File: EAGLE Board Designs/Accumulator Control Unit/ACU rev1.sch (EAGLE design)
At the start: 187 parts, among them J1 CONNECTOR-CAN_MF_T_V_, J2 CONNECTOR-8_MF_T_V_, J3 CONNECTOR-8_MF_T_V_, J4 CONNECTOR-2_MF_T_V_, J5 CONNECTOR-12_MF_T_V_, Q1 TRANSISTOR_N_MOS__PMV15ENEA, Q2 TRANSISTOR_N_MOS__PMV15ENEA, T1 TRANSFORMER_HM2112ZNLT_AIRGAP, U10 OPAMP_1_CHANNEL_OPA991, U11 LOGICGATE_AND_DCK3, U12 OPAMP_1_CHANNEL_OPA991, U13 OPAMP_1_CHANNEL_OPA991, U14 OPAMP_1_CHANNEL_OPA991, U15 LOGICGATE_AND_DCK3, U18 OPAMP_1_CHANNEL_OPA991, U19 MAX7404, U2 ADG1423, U20 OPAMP_1_CHANNEL_OPA991, U22 OPAMP_1_CHANNEL_OPA991, U25 TCAN1051HQV-Q1, U26 MAX7404, U27 OPAMP_1_CHANNEL_OPA991, U28 MAX7404, U29 OPAMP_1_CHANNEL_OPA991, U3 LM555, U30 MAX7404, U4 OPAMP_1_CHANNEL_OPA991, U5 LTC6820, U6 ADM823, U7 OPAMP_1_CHANNEL_OPA991, U8 LOGICGATE_AND_DCK3, U9 OPAMP_1_CHANNEL_OPA991

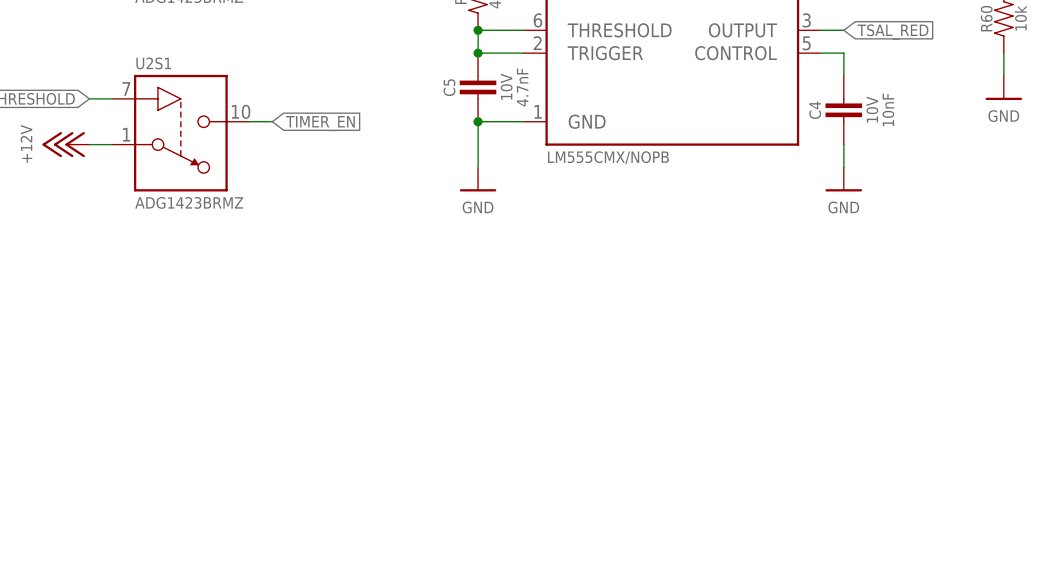
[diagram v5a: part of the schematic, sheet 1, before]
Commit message: Corrections
Added isolation barrier line
moved LTC6820 near teensy
moved precharger near connector
shdn traces now 20 mil
removed unneeded vias near 3.3V reg
mvoed caps of vregs inside keepouts
added 0603 LEDs for TSAL
mapped can tx and rx to D3 and D4 for compatibility with Teensy 3.2
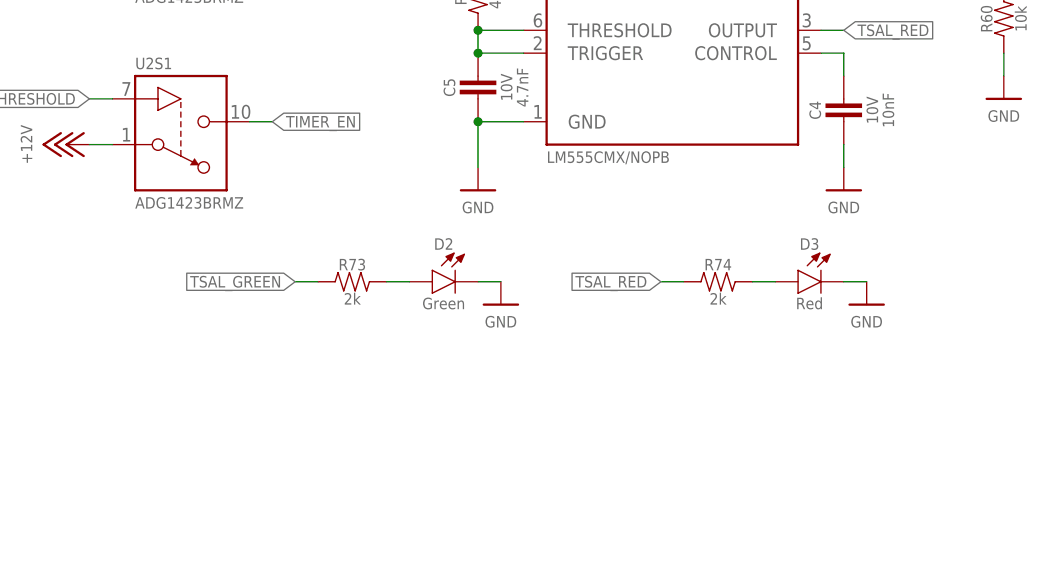
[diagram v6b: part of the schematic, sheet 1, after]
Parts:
- added D2: LED_0603_GREEN, HyTechDevices:LED_0603_GREEN
- added D3: LED_0603_RED, HyTechDevices:LED_0603_RED
- added R73, R74: RESISTOR_0603_2K, HyTechDevices:RESISTOR_0603_2K
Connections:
- new net N$29: A1.(CTX1)D1, A1.D3, U25.TXD
- new net N$46: D3.A, R74.2
- net GND: now also D2.C, D3.C
- net N$24: now also D2.A, R73.2; no longer A1.(CTX1)D1, U25.TXD
- net N$25: now also A1.D4
- net TEENSY_OK: now also A1.D6; no longer A1.D5
- net TSAL_GREEN: now also R73.1
- net TSAL_RED: now also R74.1
- net WATCHDOG_INPUT: now also A1.D5; no longer A1.D4
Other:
- moved on the sheet: WATCHDOG_OK
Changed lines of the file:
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@@
 <drawing>
 <settings>
-<setting alwaysvectorfont="yes"/>
+<setting alwaysvectorfont="no"/>
 <setting verticaltext="up"/>
 </settings>
@@
 <part name="IMD_OK" library="HyTechDevices - Copy" deviceset="LED_?_*" device="0603" technology="ORANGE"/>
 <part name="R72" library="HyTechDevices" deviceset="RESISTOR_?_*" device="0603" technology="2K"/>
+<part name="D2" library="HyTechDevices" deviceset="LED_?_*" device="0603" technology="GREEN"/>
+<part name="D3" library="HyTechDevices" deviceset="LED_?_*" device="0603" technology="RED"/>
+<part name="R73" library="HyTechDevices" deviceset="RESISTOR_?_*" device="0603" technology="2K"/>
+<part name="R74" library="HyTechDevices" deviceset="RESISTOR_?_*" device="0603" technology="2K"/>
+<part name="P48" library="HyTechSupplies" deviceset="GND" device=""/>
+<part name="P49" library="HyTechSupplies" deviceset="GND" device=""/>
 </parts>
 <sheets>
@@
 <attribute name="MPN" x="17.78" y="79.502" size="1.27" layer="95" align="top-left"/>
 </instance>
+<instance part="D2" gate="LED" x="190.5" y="66.04" smashed="yes">
+<attribute name="COLOR" x="189.23" y="64.262" size="1.27" layer="95" align="top-center"/>
+<attribute name="NAME" x="189.23" y="69.596" size="1.27" layer="96" align="bottom-center"/>
+</instance>
+<instance part="D3" gate="LED" x="231.14" y="66.04" smashed="yes">
+<attribute name="COLOR" x="229.87" y="64.262" size="1.27" layer="95" align="top-center"/>
+<attribute name="NAME" x="229.87" y="69.596" size="1.27" layer="96" align="bottom-center"/>
+</instance>
+<instance part="R73" gate="G$1" x="180.34" y="66.04" smashed="yes">
+<attribute name="NAME" x="179.07" y="67.31" size="1.27" layer="95" align="bottom-center"/>
+<attribute name="RESISTANCE" x="179.07" y="64.77" size="1.27" layer="96" align="top-center"/>
+</instance>
+<instance part="R74" gate="G$1" x="220.98" y="66.04" smashed="yes">
+<attribute name="NAME" x="219.71" y="67.31" size="1.27" layer="95" align="bottom-center"/>
+<attribute name="RESISTANCE" x="219.71" y="64.77" size="1.27" layer="96" align="top-center"/>
+</instance>
+<instance part="P48" gate="1" x="195.58" y="63.5" smashed="yes">
+<attribute name="VALUE" x="195.58" y="62.23" size="1.27" layer="96" align="top-center"/>
+</instance>
+<instance part="P49" gate="1" x="236.22" y="63.5" smashed="yes">
+<attribute name="VALUE" x="236.22" y="62.23" size="1.27" layer="96" align="top-center"/>
+</instance>
 </instances>
 <busses>
@@
 <pinref part="3.3V" gate="LED" pin="C"/>
 </segment>
+<segment>
+<pinref part="D2" gate="LED" pin="C"/>
+<wire x1="193.04" y1="66.04" x2="195.58" y2="66.04" width="0.1524" layer="91"/>
+<pinref part="P48" gate="1" pin="GND"/>
+</segment>
+<segment>
+<pinref part="D3" gate="LED" pin="C"/>
+<wire x1="233.68" y1="66.04" x2="236.22" y2="66.04" width="0.1524" layer="91"/>
+<pinref part="P49" gate="1" pin="GND"/>
+</segment>
 </net>
 <net name="+12V" class="0">
@@
 <label x="233.68" y="93.98" size="1.27" layer="95" xref="yes"/>
 </segment>
+<segment>
+<pinref part="R74" gate="G$1" pin="1"/>
+<wire x1="215.9" y1="66.04" x2="213.36" y2="66.04" width="0.1524" layer="91"/>
+<label x="213.36" y="66.04" size="1.27" layer="95" rot="R180" xref="yes"/>
+</segment>
 </net>
 <net name="TSAL_GREEN" class="0">
@@
 <label x="170.18" y="101.6" size="1.27" layer="95" xref="yes"/>
 </segment>
+<segment>
+<pinref part="R73" gate="G$1" pin="1"/>
+<wire x1="175.26" y1="66.04" x2="172.72" y2="66.04" width="0.1524" layer="91"/>
+<label x="172.72" y="66.04" size="1.27" layer="95" rot="R180" xref="yes"/>
+</segment>
 </net>
 <net name="12VIN" class="0">
@@
 </segment>
 </net>
+<net name="N$24" class="0">
+<segment>
+<pinref part="D2" gate="LED" pin="A"/>
+<wire x1="185.42" y1="66.04" x2="182.88" y2="66.04" width="0.1524" layer="91"/>
+<pinref part="R73" gate="G$1" pin="2"/>
+</segment>
+</net>
+<net name="N$46" class="0">
+<segment>
+<pinref part="D3" gate="LED" pin="A"/>
+<wire x1="226.06" y1="66.04" x2="223.52" y2="66.04" width="0.1524" layer="91"/>
+<pinref part="R74" gate="G$1" pin="2"/>
+</segment>
+</net>
 </nets>
 </sheet>
@@
 <attribute name="CAPACITANCE" x="135.89" y="181.102" size="1.27" layer="96" align="top-center"/>
 </instance>
-<instance part="WATCHDOG_OK" gate="G$1" x="78.74" y="147.32" smashed="yes">
-<attribute name="NAME" x="76.2" y="149.098" size="1.27" layer="95"/>
-<attribute name="MPN" x="76.2" y="145.542" size="1.27" layer="95" align="top-left"/>
+<instance part="WATCHDOG_OK" gate="G$1" x="91.44" y="147.32" smashed="yes">
+<attribute name="NAME" x="88.9" y="149.098" size="1.27" layer="95"/>
+<attribute name="MPN" x="88.9" y="145.542" size="1.27" layer="95" align="top-left"/>
 </instance>
 </instances>
@@
 </segment>
 <segment>
-<wire x1="73.66" y1="149.86" x2="83.82" y2="149.86" width="0.1524" layer="91"/>
-<label x="88.9" y="149.86" size="1.27" layer="95" xref="yes"/>
-<pinref part="A1" gate="G$1" pin="D4"/>
+<label x="88.9" y="152.4" size="1.27" layer="95" xref="yes"/>
 <pinref part="WATCHDOG_OK" gate="G$1" pin="P$1"/>
-<wire x1="83.82" y1="149.86" x2="88.9" y2="149.86" width="0.1524" layer="91"/>
-<wire x1="83.82" y1="149.86" x2="83.82" y2="147.32" width="0.1524" layer="91"/>
-<wire x1="83.82" y1="147.32" x2="81.28" y2="147.32" width="0.1524" layer="91"/>
-<junction x="83.82" y="149.86"/>
+<wire x1="83.82" y1="152.4" x2="88.9" y2="152.4" width="0.1524" layer="91"/>
+<wire x1="83.82" y1="152.4" x2="83.82" y2="147.32" width="0.1524" layer="91"/>
+<wire x1="83.82" y1="147.32" x2="93.98" y2="147.32" width="0.1524" layer="91"/>
+<pinref part="A1" gate="G$1" pin="D5"/>
+<wire x1="73.66" y1="152.4" x2="83.82" y2="152.4" width="0.1524" layer="91"/>
+<junction x="83.82" y="152.4"/>
 </segment>
 </net>
@@
 </segment>
 <segment>
-<wire x1="73.66" y1="152.4" x2="88.9" y2="152.4" width="0.1524" layer="91"/>
-<label x="88.9" y="152.4" size="1.27" layer="95" xref="yes"/>
-<pinref part="A1" gate="G$1" pin="D5"/>
+<pinref part="A1" gate="G$1" pin="D6"/>
+<wire x1="73.66" y1="154.94" x2="88.9" y2="154.94" width="0.1524" layer="91"/>
+<label x="88.9" y="154.94" size="1.27" layer="95" xref="yes"/>
 </segment>
 </net>
@@
 </segment>
 </net>
-<net name="N$24" class="0">
-<segment>
-<pinref part="A1" gate="G$1" pin="(CTX1)D1"/>
-<wire x1="73.66" y1="142.24" x2="106.68" y2="142.24" width="0.1524" layer="91"/>
-<wire x1="106.68" y1="142.24" x2="106.68" y2="114.3" width="0.1524" layer="91"/>
-<pinref part="U25" gate="G$1" pin="TXD"/>
-<wire x1="106.68" y1="114.3" x2="124.46" y2="114.3" width="0.1524" layer="91"/>
-</segment>
-</net>
 <net name="N$25" class="0">
 <segment>
@@
 <wire x1="104.14" y1="111.76" x2="104.14" y2="139.7" width="0.1524" layer="91"/>
 <pinref part="A1" gate="G$1" pin="(CRX1)D0"/>
-<wire x1="104.14" y1="139.7" x2="73.66" y2="139.7" width="0.1524" layer="91"/>
+<wire x1="104.14" y1="139.7" x2="78.74" y2="139.7" width="0.1524" layer="91"/>
+<pinref part="A1" gate="G$1" pin="D4"/>
+<wire x1="78.74" y1="139.7" x2="73.66" y2="139.7" width="0.1524" layer="91"/>
+<wire x1="73.66" y1="149.86" x2="78.74" y2="149.86" width="0.1524" layer="91"/>
+<wire x1="78.74" y1="149.86" x2="78.74" y2="139.7" width="0.1524" layer="91"/>
+<junction x="78.74" y="139.7"/>
 </segment>
 </net>
@@
 </segment>
 </net>
+<net name="N$29" class="0">
+<segment>
+<pinref part="A1" gate="G$1" pin="D3"/>
+<wire x1="73.66" y1="147.32" x2="76.2" y2="147.32" width="0.1524" layer="91"/>
+<pinref part="A1" gate="G$1" pin="(CTX1)D1"/>
+<wire x1="73.66" y1="142.24" x2="76.2" y2="142.24" width="0.1524" layer="91"/>
+<wire x1="76.2" y1="142.24" x2="106.68" y2="142.24" width="0.1524" layer="91"/>
+<wire x1="106.68" y1="142.24" x2="106.68" y2="114.3" width="0.1524" layer="91"/>
+<pinref part="U25" gate="G$1" pin="TXD"/>
+<wire x1="106.68" y1="114.3" x2="124.46" y2="114.3" width="0.1524" layer="91"/>
+<wire x1="76.2" y1="147.32" x2="76.2" y2="142.24" width="0.1524" layer="91"/>
+<junction x="76.2" y="142.24"/>
+</segment>
+</net>

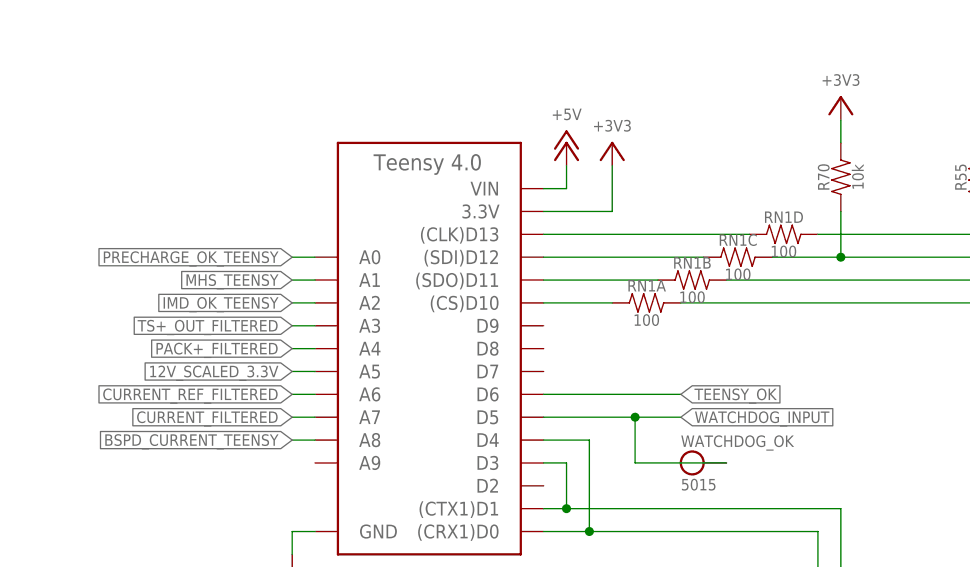
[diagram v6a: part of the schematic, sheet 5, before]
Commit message: adjust teensy position
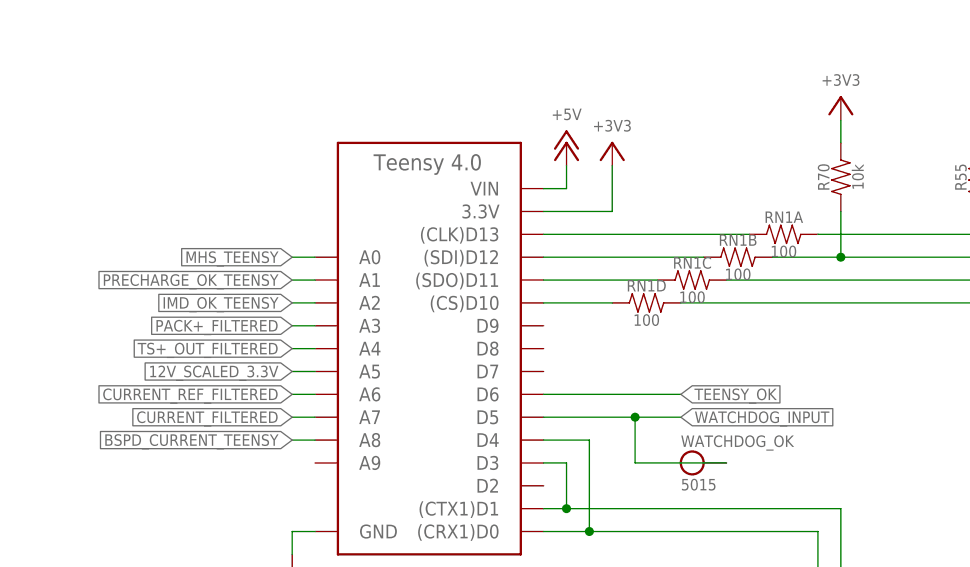
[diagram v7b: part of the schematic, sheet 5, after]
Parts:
- RN1: device HyTechDevices:RESISTOR_NETWORK_4_100 -> HyTechDevices - Copy:RESISTOR_NETWORK_4_100
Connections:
- net CS_LTC_6820: now also RN1D.2; no longer RN1A.2
- net MHS_TEENSY: now also A1.A0; no longer A1.A1
- net N$13: now also RN1A.2; no longer RN1D.2
- net N$15: now also RN1B.2; no longer RN1C.2
- net N$18: now also RN1C.2; no longer RN1B.2
- net N$19: now also RN1D.1; no longer RN1A.1
- net N$21: now also RN1C.1; no longer RN1B.1
- net N$43: now also RN1B.1; no longer RN1C.1
- net N$44: now also RN1A.1; no longer RN1D.1
- net PACK+_FILTERED: now also A1.A3; no longer A1.A4
- net PRECHARGE_OK_TEENSY: now also A1.A1; no longer A1.A0
- net TS+_OUT_FILTERED: now also A1.A4; no longer A1.A3
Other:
- moved on the sheet: RN1A, RN1B, RN1C, RN1D
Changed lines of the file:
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@@
 <drawing>
 <settings>
-<setting alwaysvectorfont="no"/>
+<setting alwaysvectorfont="yes"/>
 <setting verticaltext="up"/>
 </settings>
@@
 <part name="R62" library="HyTechDevices" deviceset="RESISTOR_?_*" device="0603" technology="10K"/>
 <part name="GND6" library="supply1" deviceset="GND" device=""/>
-<part name="RN1" library="HyTechDevices" deviceset="RESISTOR_NETWORK_4_*" device="" technology="100"/>
 <part name="Q2" library="HyTechDevices" deviceset="TRANSISTOR_N_MOS_?_*" device="" technology="PMV15ENEA"/>
 <part name="P10" library="HyTechSupplies" deviceset="GND" device=""/>
@@
 <part name="P48" library="HyTechSupplies" deviceset="GND" device=""/>
 <part name="P49" library="HyTechSupplies" deviceset="GND" device=""/>
+<part name="RN1" library="HyTechDevices - Copy" deviceset="RESISTOR_NETWORK_4_*" device="" technology="100"/>
 </parts>
 <sheets>
@@
 <attribute name="RESISTANCE" x="123.19" y="179.07" size="1.27" layer="96" rot="R90" align="top-center"/>
 </instance>
-<instance part="RN1" gate="A" x="86.36" y="165.1" smashed="yes">
-<attribute name="NAME" x="85.09" y="166.37" size="1.27" layer="95" align="bottom-center"/>
-<attribute name="RESISTANCE" x="85.09" y="163.83" size="1.27" layer="96" align="top-center"/>
-</instance>
-<instance part="RN1" gate="B" x="91.44" y="167.64" smashed="yes">
-<attribute name="NAME" x="90.17" y="168.91" size="1.27" layer="95" align="bottom-center"/>
-<attribute name="RESISTANCE" x="90.17" y="166.37" size="1.27" layer="96" align="top-center"/>
-</instance>
-<instance part="RN1" gate="C" x="96.52" y="170.18" smashed="yes">
-<attribute name="NAME" x="95.25" y="171.45" size="1.27" layer="95" align="bottom-center"/>
-<attribute name="RESISTANCE" x="95.25" y="168.91" size="1.27" layer="96" align="top-center"/>
-</instance>
-<instance part="RN1" gate="D" x="101.6" y="172.72" smashed="yes">
-<attribute name="NAME" x="100.33" y="173.99" size="1.27" layer="95" align="bottom-center"/>
-<attribute name="RESISTANCE" x="100.33" y="171.45" size="1.27" layer="96" align="top-center"/>
-</instance>
 <instance part="R43" gate="G$1" x="71.12" y="86.36" smashed="yes">
 <attribute name="NAME" x="69.85" y="87.63" size="1.27" layer="95" align="bottom-center"/>
@@
 <attribute name="MPN" x="88.9" y="145.542" size="1.27" layer="95" align="top-left"/>
 </instance>
+<instance part="RN1" gate="A" x="101.6" y="172.72" smashed="yes">
+<attribute name="NAME" x="100.33" y="173.99" size="1.27" layer="95" align="bottom-center"/>
+<attribute name="RESISTANCE" x="100.33" y="171.45" size="1.27" layer="96" align="top-center"/>
+</instance>
+<instance part="RN1" gate="B" x="96.52" y="170.18" smashed="yes">
+<attribute name="NAME" x="95.25" y="171.45" size="1.27" layer="95" align="bottom-center"/>
+<attribute name="RESISTANCE" x="95.25" y="168.91" size="1.27" layer="96" align="top-center"/>
+</instance>
+<instance part="RN1" gate="C" x="91.44" y="167.64" smashed="yes">
+<attribute name="NAME" x="90.17" y="168.91" size="1.27" layer="95" align="bottom-center"/>
+<attribute name="RESISTANCE" x="90.17" y="166.37" size="1.27" layer="96" align="top-center"/>
+</instance>
+<instance part="RN1" gate="D" x="86.36" y="165.1" smashed="yes">
+<attribute name="NAME" x="85.09" y="166.37" size="1.27" layer="95" align="bottom-center"/>
+<attribute name="RESISTANCE" x="85.09" y="163.83" size="1.27" layer="96" align="top-center"/>
+</instance>
 </instances>
 <busses>
@@
 </segment>
 <segment>
-<wire x1="48.26" y1="170.18" x2="45.72" y2="170.18" width="0.1524" layer="91"/>
-<label x="45.72" y="170.18" size="1.27" layer="95" rot="R180" xref="yes"/>
-<pinref part="A1" gate="G$1" pin="A0"/>
+<wire x1="48.26" y1="167.64" x2="45.72" y2="167.64" width="0.1524" layer="91"/>
+<label x="45.72" y="167.64" size="1.27" layer="95" rot="R180" xref="yes"/>
+<pinref part="A1" gate="G$1" pin="A1"/>
 </segment>
 </net>
@@
 <junction x="121.92" y="165.1"/>
 <wire x1="88.9" y1="165.1" x2="121.92" y2="165.1" width="0.1524" layer="91"/>
-<pinref part="RN1" gate="A" pin="2"/>
 <pinref part="U5" gate="G$1" pin="!CS"/>
+<pinref part="RN1" gate="D" pin="2"/>
 </segment>
 </net>
@@
 </segment>
 <segment>
-<pinref part="A1" gate="G$1" pin="A5"/>
 <wire x1="48.26" y1="157.48" x2="45.72" y2="157.48" width="0.1524" layer="91"/>
 <label x="45.72" y="157.48" size="1.27" layer="95" rot="R180" xref="yes"/>
+<pinref part="A1" gate="G$1" pin="A5"/>
 </segment>
 </net>
@@
 <pinref part="A1" gate="G$1" pin="(SDO)D11"/>
 <wire x1="73.66" y1="167.64" x2="86.36" y2="167.64" width="0.1524" layer="91"/>
-<pinref part="RN1" gate="B" pin="1"/>
+<pinref part="RN1" gate="C" pin="1"/>
 </segment>
 </net>
@@
 <pinref part="A1" gate="G$1" pin="(SDI)D12"/>
 <wire x1="91.44" y1="170.18" x2="73.66" y2="170.18" width="0.1524" layer="91"/>
-<pinref part="RN1" gate="C" pin="1"/>
+<pinref part="RN1" gate="B" pin="1"/>
 </segment>
 </net>
@@
 <pinref part="A1" gate="G$1" pin="(CLK)D13"/>
 <wire x1="73.66" y1="172.72" x2="96.52" y2="172.72" width="0.1524" layer="91"/>
-<pinref part="RN1" gate="D" pin="1"/>
+<pinref part="RN1" gate="A" pin="1"/>
 </segment>
 </net>
@@
 </segment>
 <segment>
-<wire x1="48.26" y1="167.64" x2="45.72" y2="167.64" width="0.1524" layer="91"/>
-<label x="45.72" y="167.64" size="1.27" layer="95" rot="R180" xref="yes"/>
-<pinref part="A1" gate="G$1" pin="A1"/>
+<wire x1="48.26" y1="170.18" x2="45.72" y2="170.18" width="0.1524" layer="91"/>
+<label x="45.72" y="170.18" size="1.27" layer="95" rot="R180" xref="yes"/>
+<pinref part="A1" gate="G$1" pin="A0"/>
 </segment>
 </net>
@@
 <pinref part="A1" gate="G$1" pin="(CS)D10"/>
 <wire x1="73.66" y1="165.1" x2="81.28" y2="165.1" width="0.1524" layer="91"/>
-<pinref part="RN1" gate="A" pin="1"/>
+<pinref part="RN1" gate="D" pin="1"/>
 </segment>
 </net>
@@
 <net name="N$13" class="0">
 <segment>
-<pinref part="RN1" gate="D" pin="2"/>
 <wire x1="104.14" y1="172.72" x2="132.08" y2="172.72" width="0.1524" layer="91"/>
 <pinref part="U5" gate="G$1" pin="CLK"/>
+<pinref part="RN1" gate="A" pin="2"/>
 </segment>
 </net>
 <net name="N$15" class="0">
 <segment>
-<pinref part="RN1" gate="C" pin="2"/>
 <wire x1="99.06" y1="170.18" x2="106.68" y2="170.18" width="0.1524" layer="91"/>
 <wire x1="106.68" y1="170.18" x2="132.08" y2="170.18" width="0.1524" layer="91"/>
@@
 <pinref part="R70" gate="G$1" pin="1"/>
 <pinref part="U5" gate="G$1" pin="SDO"/>
+<pinref part="RN1" gate="B" pin="2"/>
 </segment>
 </net>
@@
 <segment>
 <wire x1="93.98" y1="167.64" x2="132.08" y2="167.64" width="0.1524" layer="91"/>
-<pinref part="RN1" gate="B" pin="2"/>
 <pinref part="U5" gate="G$1" pin="SDI"/>
+<pinref part="RN1" gate="C" pin="2"/>
 </segment>
 </net>
@@
 </segment>
 </net>
-<net name="TS+_OUT_FILTERED" class="0">
-<segment>
-<wire x1="48.26" y1="162.56" x2="45.72" y2="162.56" width="0.1524" layer="91"/>
-<label x="45.72" y="162.56" size="1.27" layer="95" rot="R180" xref="yes"/>
-<pinref part="A1" gate="G$1" pin="A3"/>
-</segment>
-</net>
-<net name="PACK+_FILTERED" class="0">
-<segment>
-<wire x1="48.26" y1="160.02" x2="45.72" y2="160.02" width="0.1524" layer="91"/>
-<label x="45.72" y="160.02" size="1.27" layer="95" rot="R180" xref="yes"/>
-<pinref part="A1" gate="G$1" pin="A4"/>
-</segment>
-</net>
 <net name="N$29" class="0">
 <segment>
@@
 </segment>
 </net>
+<net name="TS+_OUT_FILTERED" class="0">
+<segment>
+<wire x1="48.26" y1="160.02" x2="45.72" y2="160.02" width="0.1524" layer="91"/>
+<label x="45.72" y="160.02" size="1.27" layer="95" rot="R180" xref="yes"/>
+<pinref part="A1" gate="G$1" pin="A4"/>
+</segment>
+</net>
+<net name="PACK+_FILTERED" class="0">
+<segment>
+<wire x1="48.26" y1="162.56" x2="45.72" y2="162.56" width="0.1524" layer="91"/>
+<label x="45.72" y="162.56" size="1.27" layer="95" rot="R180" xref="yes"/>
+<pinref part="A1" gate="G$1" pin="A3"/>
+</segment>
+</net>
